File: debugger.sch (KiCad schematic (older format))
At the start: 7 parts, among them J2 USB_B_Micro, U7 STM32F042F6Px

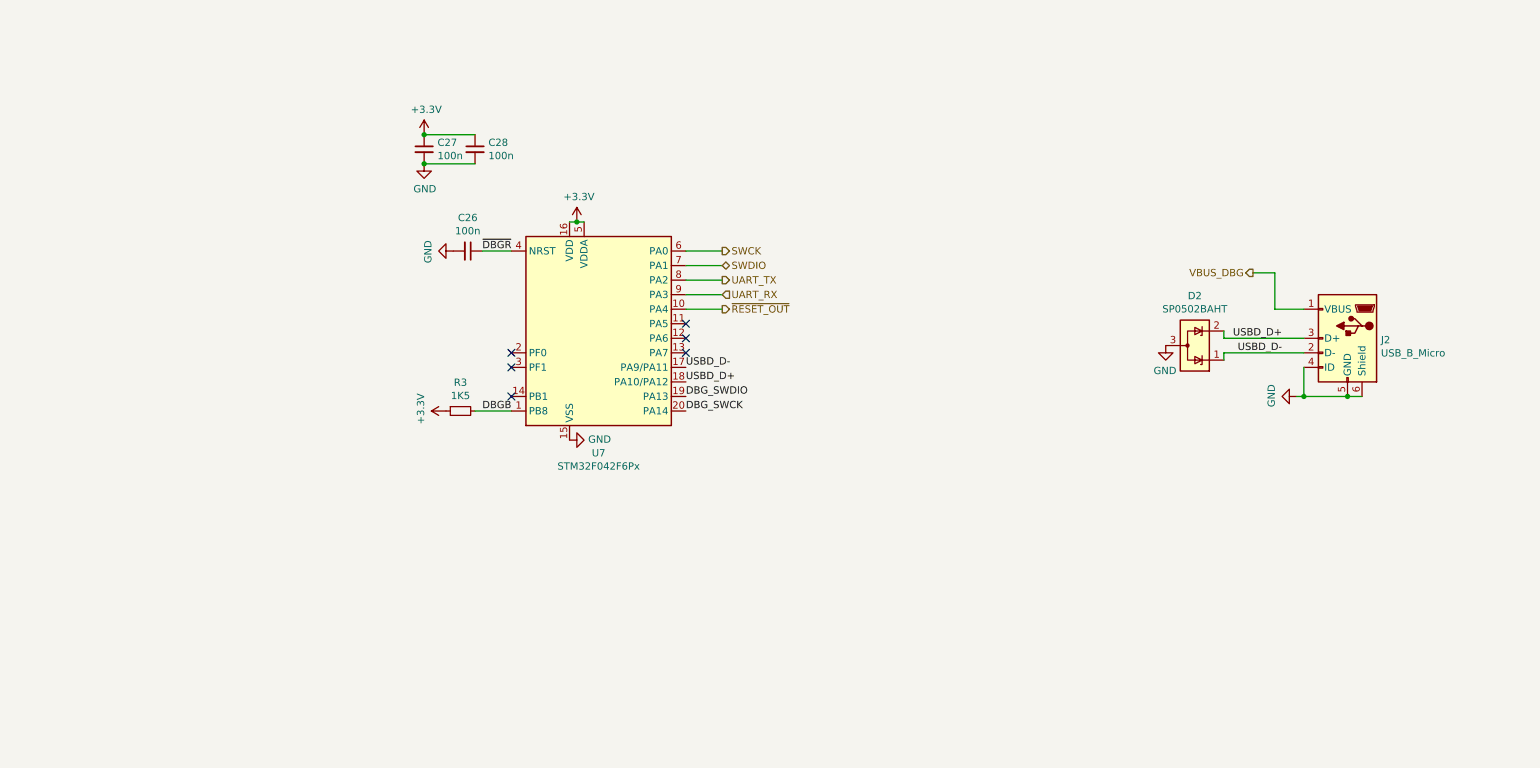
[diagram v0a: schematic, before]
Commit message: Add SWD connector for cortex-m7, SWD poggo pins and boot jumper for cmsis-dap mcu.
Signed-off-by: Martin Ribelotta <martinribelotta@gmail.com>
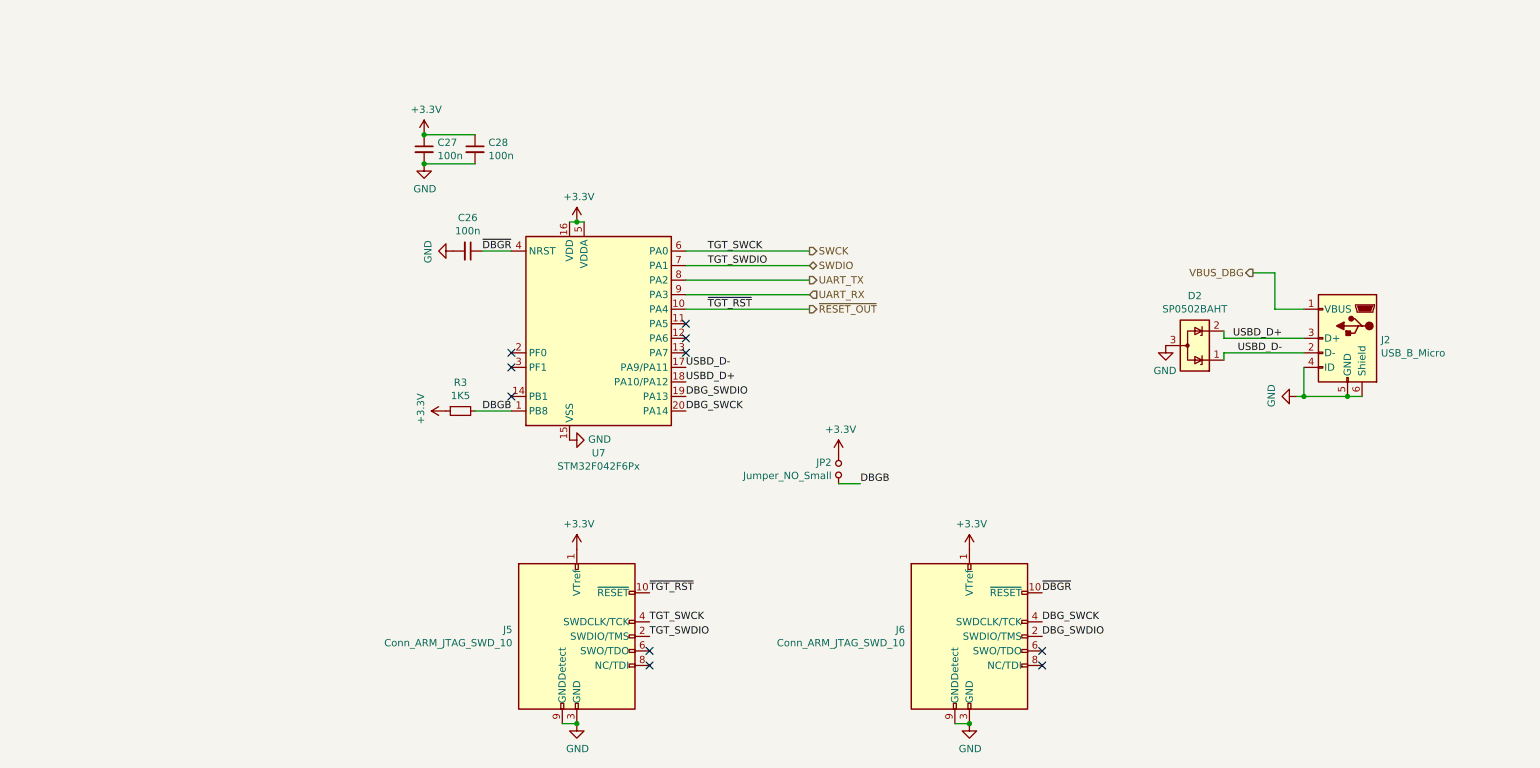
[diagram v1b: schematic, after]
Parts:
- added J5: Conn_ARM_JTAG_SWD_10, Connector_PinHeader_1.27mm:PinHeader_2x05_P1.27mm_Vertical_SMD, symbol Connector:Conn_ARM_JTAG_SWD_10
- added J6: Conn_ARM_JTAG_SWD_10, Connector:Tag-Connect_TC2050-IDC-NL_2x05_P1.27mm_Vertical, symbol Connector:Conn_ARM_JTAG_SWD_10
- added JP2: Jumper_NO_Small, Connector_PinHeader_2.54mm:PinHeader_1x02_P2.54mm_Vertical, symbol Device:Jumper_NO_Small
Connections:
- net +3V3: now also J5.1 (VTref), J6.1 (VTref), JP2.2
- net DBGB: now also JP2.1
- net DBG_SWCK: now also J6.4 (SWDCLK/TCK)
- net DBG_SWDIO: now also J6.2 (SWDIO/TMS)
- net GND: now also J5.3 (GND), J5.5 (GND), J5.9 (GNDDetect), J6.3 (GND), J6.5 (GND), J6.9 (GNDDetect)
- net SWCK: now also J5.4 (SWDCLK/TCK)
- net SWDIO: now also J5.2 (SWDIO/TMS)
- net ~DBGR: now also J6.10 (~RESET~)
- net ~RESET_OUT: now also J5.10 (~RESET~)
- no-connect marks 6 -> 10
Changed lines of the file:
@@
 	1    0    0    -1
 $EndComp
-Text HLabel 5400 2800 2    50   Output ~ 0
+Text HLabel 6000 2800 2    50   Output ~ 0
 SWCK
-Text HLabel 5400 2900 2    50   BiDi ~ 0
+Text HLabel 6000 2900 2    50   BiDi ~ 0
 SWDIO
-Wire Wire Line
-	5150 2800 5400 2800
-Wire Wire Line
-	5400 2900 5150 2900
-Text HLabel 5400 3000 2    50   Output ~ 0
+Text HLabel 6000 3000 2    50   Output ~ 0
 UART_TX
-Text HLabel 5400 3100 2    50   Input ~ 0
+Text HLabel 6000 3100 2    50   Input ~ 0
 UART_RX
-Wire Wire Line
-	5400 3000 5150 3000
-Wire Wire Line
-	5150 3100 5400 3100
 NoConn ~ 5150 3300
 NoConn ~ 5150 3400
-Text HLabel 5400 3200 2    50   Output ~ 0
+Text HLabel 6000 3200 2    50   Output ~ 0
 ~RESET_OUT
-Wire Wire Line
-	5400 3200 5150 3200
 NoConn ~ 5150 3500
 Text Label 5150 3700 0    50   ~ 0
@@
 Wire Wire Line
 	9200 3200 9400 3200
+Text Label 7600 5450 0    50   ~ 0
+DBG_SWDIO
+Text Label 7600 5350 0    50   ~ 0
+DBG_SWCK
+Text Label 7600 5150 0    50   ~ 0
+~DBGR
+Text Label 6350 4400 0    50   ~ 0
+DBGB
+$Comp
+L Device:Jumper_NO_Small JP2
+U 1 1 60341504
+P 6200 4300
+F 0 "JP2" V 6246 4348 50  0000 L CNN
+F 1 "Jumper_NO_Small" V 6155 4348 50  0000 L CNN
+F 2 "Connector_PinHeader_2.54mm:PinHeader_1x02_P2.54mm_Vertical" H 6200 4300 50  0001 C CNN
+F 3 "~" H 6200 4300 50  0001 C CNN
+	1    6200 4300
+	0    -1   -1   0
+$EndComp
+Wire Wire Line
+	6200 4400 6350 4400
+$Comp
+L power:+3V3 #PWR?
+U 1 1 60346736
+P 6200 4200
+AR Path="/60346736" Ref="#PWR?"  Part="1"
+AR Path="/60158DDC/60346736" Ref="#PWR052"  Part="1"
+F 0 "#PWR052" H 6200 4050 50  0001 C CNN
+F 1 "+3.3V" H 6215 4373 50  0000 C CNN
+F 2 "" H 6200 4200 50  0000 C CNN
+F 3 "" H 6200 4200 50  0000 C CNN
+	1    6200 4200
+	1    0    0    -1
+$EndComp
+$Comp
+L Connector:Conn_ARM_JTAG_SWD_10 J5
+U 1 1 60372EBF
+P 4400 5450
+F 0 "J5" H 3957 5496 50  0000 R CNN
+F 1 "Conn_ARM_JTAG_SWD_10" H 3957 5405 50  0000 R CNN
+F 2 "Connector_PinHeader_1.27mm:PinHeader_2x05_P1.27mm_Vertical_SMD" H 4400 5450 50  0001 C CNN
+F 3 "http://infocenter.arm.com/help/topic/com.arm.doc.ddi0314h/DDI0314H_coresight_components_trm.pdf" V 4050 4200 50  0001 C CNN
+	1    4400 5450
+	1    0    0    -1
+$EndComp
+$Comp
+L power:+3V3 #PWR?
+U 1 1 60372EC5
+P 4400 4850
+AR Path="/60372EC5" Ref="#PWR?"  Part="1"
+AR Path="/60158DDC/60372EC5" Ref="#PWR026"  Part="1"
+F 0 "#PWR026" H 4400 4700 50  0001 C CNN
+F 1 "+3.3V" H 4415 5023 50  0000 C CNN
+F 2 "" H 4400 4850 50  0000 C CNN
+F 3 "" H 4400 4850 50  0000 C CNN
+	1    4400 4850
+	1    0    0    -1
+$EndComp
+$Comp
+L power:GND #PWR?
+U 1 1 60372ECB
+P 4400 6050
+AR Path="/60372ECB" Ref="#PWR?"  Part="1"
+AR Path="/60158DDC/60372ECB" Ref="#PWR029"  Part="1"
+F 0 "#PWR029" H 4400 5800 50  0001 C CNN
+F 1 "GND" H 4405 5877 50  0000 C CNN
+F 2 "" H 4400 6050 50  0000 C CNN
+F 3 "" H 4400 6050 50  0000 C CNN
+	1    4400 6050
+	1    0    0    -1
+$EndComp
+Wire Wire Line
+	4300 6050 4400 6050
+Connection ~ 4400 6050
+Wire Wire Line
+	5150 2800 6000 2800
+Wire Wire Line
+	5150 2900 6000 2900
+Wire Wire Line
+	5150 3000 6000 3000
+Wire Wire Line
+	5150 3100 6000 3100
+Wire Wire Line
+	5150 3200 6000 3200
+Text Label 5300 2800 0    50   ~ 0
+TGT_SWCK
+Text Label 5300 2900 0    50   ~ 0
+TGT_SWDIO
+Text Label 5300 3200 0    50   ~ 0
+~TGT_RST
+Text Label 4900 5350 0    50   ~ 0
+TGT_SWCK
+Text Label 4900 5450 0    50   ~ 0
+TGT_SWDIO
+NoConn ~ 4900 5550
+NoConn ~ 4900 5650
+Text Label 4900 5150 0    50   ~ 0
+~TGT_RST
+$Comp
+L Connector:Conn_ARM_JTAG_SWD_10 J6
+U 1 1 6037A7B7
+P 7100 5450
+F 0 "J6" H 6657 5496 50  0000 R CNN
+F 1 "Conn_ARM_JTAG_SWD_10" H 6657 5405 50  0000 R CNN
+F 2 "Connector:Tag-Connect_TC2050-IDC-NL_2x05_P1.27mm_Vertical" H 7100 5450 50  0001 C CNN
+F 3 "http://infocenter.arm.com/help/topic/com.arm.doc.ddi0314h/DDI0314H_coresight_components_trm.pdf" V 6750 4200 50  0001 C CNN
+	1    7100 5450
+	1    0    0    -1
+$EndComp
+NoConn ~ 7600 5550
+NoConn ~ 7600 5650
+$Comp
+L power:GND #PWR?
+U 1 1 6038215C
+P 7100 6050
+AR Path="/6038215C" Ref="#PWR?"  Part="1"
+AR Path="/60158DDC/6038215C" Ref="#PWR061"  Part="1"
+F 0 "#PWR061" H 7100 5800 50  0001 C CNN
+F 1 "GND" H 7105 5877 50  0000 C CNN
+F 2 "" H 7100 6050 50  0000 C CNN
+F 3 "" H 7100 6050 50  0000 C CNN
+	1    7100 6050
+	1    0    0    -1
+$EndComp
+Wire Wire Line
+	7100 6050 7000 6050
+Connection ~ 7100 6050
+$Comp
+L power:+3V3 #PWR?
+U 1 1 60383929
+P 7100 4850
+AR Path="/60383929" Ref="#PWR?"  Part="1"
+AR Path="/60158DDC/60383929" Ref="#PWR053"  Part="1"
+F 0 "#PWR053" H 7100 4700 50  0001 C CNN
+F 1 "+3.3V" H 7115 5023 50  0000 C CNN
+F 2 "" H 7100 4850 50  0000 C CNN
+F 3 "" H 7100 4850 50  0000 C CNN
+	1    7100 4850
+	1    0    0    -1
+$EndComp
 $EndSCHEMATC

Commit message: Replace non stocked components.
 - Redesign 5V/3.3V using TPS6216xDSGT
 - Use bigger crystal (move to 5031 case)
 - Change some components parts

Signed-off-by: Martin Ribelotta <martinribelotta@gmail.com>
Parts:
- C26, C27, C28: DESCRIPTION (none) -> Capacitor 100n 0603
- D2: DESCRIPTION (none) -> SP0502BAHT
- J2: DESCRIPTION (none) -> USB Micro B Molex 47346-0001
- R3: DESCRIPTION (none) -> Resistor 1.5K 0603
- U7: DESCRIPTION (none) -> STM32F042F6P*
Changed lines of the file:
@@
 F 2 "Package_SO:TSSOP-20_4.4x6.5mm_P0.65mm" H 4050 2600 50  0001 R CNN
 F 3 "http://www.st.com/st-web-ui/static/active/en/resource/technical/document/datasheet/DM00105814.pdf" H 4550 3300 50  0001 C CNN
+F 4 "STM32F042F6P*" H 4550 3300 50  0001 C CNN "DESCRIPTION"
 	1    4550 3300
 	1    0    0    -1
@@
 F 2 "Package_TO_SOT_SMD:SOT-23" H 8875 3400 50  0001 L CNN
 F 3 "http://www.littelfuse.com/~/media/files/littelfuse/technical%20resources/documents/data%20sheets/sp05xxba.pdf" H 8775 3575 50  0001 C CNN
+F 4 "SP0502BAHT" H 8650 3450 50  0001 C CNN "DESCRIPTION"
 	1    8650 3450
 	0    1    -1   0
@@
 F 2 "Capacitor_SMD:C_0603_1608Metric" H 3350 2100 50  0001 C CNN
 F 3 "~" H 3350 2100 50  0001 C CNN
+F 4 "Capacitor 100n 0603" H 3350 2100 50  0001 C CNN "DESCRIPTION"
 	1    3350 2100
 	1    0    0    -1
@@
 F 2 "Capacitor_SMD:C_0603_1608Metric" H 3700 2100 50  0001 C CNN
 F 3 "~" H 3700 2100 50  0001 C CNN
+F 4 "Capacitor 100n 0603" H 3700 2100 50  0001 C CNN "DESCRIPTION"
 	1    3700 2100
 	1    0    0    -1
@@
 F 2 "Capacitor_SMD:C_0603_1608Metric" H 3650 2800 50  0001 C CNN
 F 3 "~" H 3650 2800 50  0001 C CNN
+F 4 "Capacitor 100n 0603" H 3650 2800 50  0001 C CNN "DESCRIPTION"
 	1    3650 2800
 	0    1    -1   0
@@
 F 2 "Resistor_SMD:R_0603_1608Metric" H 3600 3900 50  0001 C CNN
 F 3 "~" H 3600 3900 50  0001 C CNN
+F 4 "Resistor 1.5K 0603" H 3600 3900 50  0001 C CNN "DESCRIPTION"
 	1    3600 3900
 	0    -1   1    0
@@
 F 2 "Connector_USB:USB_Micro-B_Molex_47346-0001" H 9850 3350 50  0001 C CNN
 F 3 "~" H 9850 3350 50  0001 C CNN
+F 4 "USB Micro B Molex 47346-0001" H 9700 3400 50  0001 C CNN "DESCRIPTION"
 	1    9700 3400
 	-1   0    0    -1

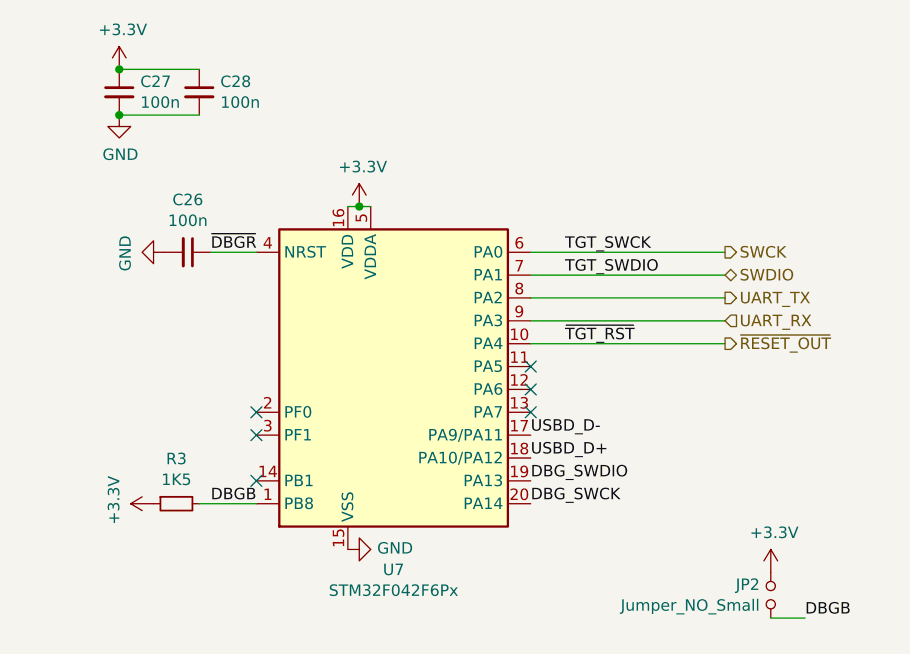
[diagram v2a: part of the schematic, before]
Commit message: Fix in design:
 - Add r-series to QSPI interfaces
 - Change vCAP from 100n to 2.2u
 - Add pullup to SWCK/DIO and nRST
 - Remove AGND/DGND separation

Signed-off-by: Martin Ribelotta <martinribelotta@gmail.com>
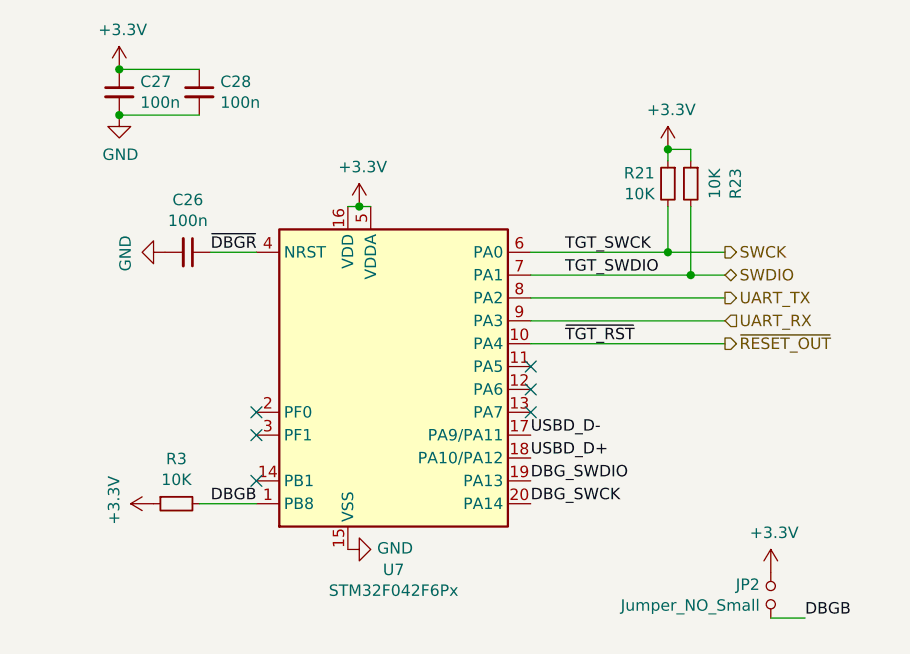
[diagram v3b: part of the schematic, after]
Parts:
- added R21, R23: 10K, Resistor_SMD:R_0603_1608Metric, symbol Device:R_Small
- R3: value 1K5 -> 10K
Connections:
- net +3V3: now also R21.1, R23.1
- net SWCK: now also R21.2
- net SWDIO: now also R23.2
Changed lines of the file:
@@
 AR Path="/60158DDC/60189E41" Ref="R3"  Part="1"
 F 0 "R3" V 3404 3900 50  0000 C CNN
-F 1 "1K5" V 3495 3900 50  0000 C CNN
+F 1 "10K" V 3495 3900 50  0000 C CNN
 F 2 "Resistor_SMD:R_0603_1608Metric" H 3600 3900 50  0001 C CNN
 F 3 "~" H 3600 3900 50  0001 C CNN
@@
 Connection ~ 4400 6050
 Wire Wire Line
-	5150 2800 6000 2800
-Wire Wire Line
-	5150 2900 6000 2900
+	5150 2800 5750 2800
+Wire Wire Line
+	5150 2900 5850 2900
 Wire Wire Line
 	5150 3000 6000 3000
@@
 	1    0    0    -1
 $EndComp
+$Comp
+L Device:R_Small R?
+U 1 1 605A9B9C
+P 5850 2500
+AR Path="/605A9B9C" Ref="R?"  Part="1"
+AR Path="/60158DDC/605A9B9C" Ref="R23"  Part="1"
+F 0 "R23" V 5654 2500 50  0000 C CNN
+F 1 "10K" V 5745 2500 50  0000 C CNN
+F 2 "Resistor_SMD:R_0603_1608Metric" H 5850 2500 50  0001 C CNN
+F 3 "~" H 5850 2500 50  0001 C CNN
+F 4 "Resistor 1.5K 0603" H 5850 2500 50  0001 C CNN "DESCRIPTION"
+	1    5850 2500
+	-1   0    0    -1
+$EndComp
+$Comp
+L Device:R_Small R?
+U 1 1 605ABFAC
+P 5750 2500
+AR Path="/605ABFAC" Ref="R?"  Part="1"
+AR Path="/60158DDC/605ABFAC" Ref="R21"  Part="1"
+F 0 "R21" H 5808 2546 50  0000 L CNN
+F 1 "10K" H 5808 2455 50  0000 L CNN
+F 2 "Resistor_SMD:R_0603_1608Metric" H 5750 2500 50  0001 C CNN
+F 3 "~" H 5750 2500 50  0001 C CNN
+F 4 "Resistor 1.5K 0603" H 5750 2500 50  0001 C CNN "DESCRIPTION"
+	1    5750 2500
+	-1   0    0    -1
+$EndComp
+Wire Wire Line
+	5750 2600 5750 2800
+Connection ~ 5750 2800
+Wire Wire Line
+	5750 2800 6000 2800
+Wire Wire Line
+	5850 2600 5850 2900
+Connection ~ 5850 2900
+Wire Wire Line
+	5850 2900 6000 2900
+$Comp
+L power:+3V3 #PWR?
+U 1 1 60617550
+P 5750 2350
+AR Path="/60617550" Ref="#PWR?"  Part="1"
+AR Path="/60158DDC/60617550" Ref="#PWR0115"  Part="1"
+F 0 "#PWR0115" H 5750 2200 50  0001 C CNN
+F 1 "+3.3V" H 5765 2523 50  0000 C CNN
+F 2 "" H 5750 2350 50  0000 C CNN
+F 3 "" H 5750 2350 50  0000 C CNN
+	1    5750 2350
+	1    0    0    -1
+$EndComp
+Wire Wire Line
+	5750 2400 5750 2350
+Wire Wire Line
+	5750 2350 5850 2350
+Wire Wire Line
+	5850 2350 5850 2400
+Connection ~ 5750 2350
 $EndSCHEMATC

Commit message: Add new BOM to octopart
TODO: PSRAM is not recognized by Octopart but is available in LCSC

Signed-off-by: Martin Ribelotta <martinribelotta@gmail.com>
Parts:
- C26, C27, C28: MANUFACTURER (none) -> Yageo; MANUFACTURER_PART_NUMBER (none) -> CC0603KRX7R9BB104
- D2: MANUFACTURER (none) -> Littlelfuse; MANUFACTURER_PART_NUMBER (none) -> SP0502BAHTG
- J2: MANUFACTURER (none) -> Molex; MANUFACTURER_PART_NUMBER (none) -> 47346-0001
- R21, R23, R3: MANUFACTURER (none) -> Yageo; MANUFACTURER_PART_NUMBER (none) -> RC0603FR-0710KL
- U7: MANUFACTURER (none) -> ST; MANUFACTURER_PART_NUMBER (none) -> STM32F042F6Px
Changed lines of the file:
@@
 F 3 "http://www.st.com/st-web-ui/static/active/en/resource/technical/document/datasheet/DM00105814.pdf" H 4550 3300 50  0001 C CNN
 F 4 "STM32F042F6P*" H 4550 3300 50  0001 C CNN "DESCRIPTION"
+F 5 "ST" H 4550 3300 50  0001 C CNN "MANUFACTURER"
+F 6 "STM32F042F6Px" H 4550 3300 50  0001 C CNN "MANUFACTURER_PART_NUMBER"
 	1    4550 3300
 	1    0    0    -1
@@
 F 3 "http://www.littelfuse.com/~/media/files/littelfuse/technical%20resources/documents/data%20sheets/sp05xxba.pdf" H 8775 3575 50  0001 C CNN
 F 4 "SP0502BAHT" H 8650 3450 50  0001 C CNN "DESCRIPTION"
+F 5 "Littlelfuse" H 8650 3450 50  0001 C CNN "MANUFACTURER"
+F 6 "SP0502BAHTG" H 8650 3450 50  0001 C CNN "MANUFACTURER_PART_NUMBER"
 	1    8650 3450
 	0    1    -1   0
@@
 F 3 "~" H 3350 2100 50  0001 C CNN
 F 4 "Capacitor 100n 0603" H 3350 2100 50  0001 C CNN "DESCRIPTION"
+F 5 "CC0603KRX7R9BB104" H 3350 2100 50  0001 C CNN "MANUFACTURER_PART_NUMBER"
+F 6 "Yageo" H 3350 2100 50  0001 C CNN "MANUFACTURER"
 	1    3350 2100
 	1    0    0    -1
@@
 F 3 "~" H 3700 2100 50  0001 C CNN
 F 4 "Capacitor 100n 0603" H 3700 2100 50  0001 C CNN "DESCRIPTION"
+F 5 "CC0603KRX7R9BB104" H 3700 2100 50  0001 C CNN "MANUFACTURER_PART_NUMBER"
+F 6 "Yageo" H 3700 2100 50  0001 C CNN "MANUFACTURER"
 	1    3700 2100
 	1    0    0    -1
@@
 F 3 "~" H 3650 2800 50  0001 C CNN
 F 4 "Capacitor 100n 0603" H 3650 2800 50  0001 C CNN "DESCRIPTION"
+F 5 "CC0603KRX7R9BB104" H 3650 2800 50  0001 C CNN "MANUFACTURER_PART_NUMBER"
+F 6 "Yageo" H 3650 2800 50  0001 C CNN "MANUFACTURER"
 	1    3650 2800
 	0    1    -1   0
@@
 F 3 "~" H 3600 3900 50  0001 C CNN
 F 4 "Resistor 1.5K 0603" H 3600 3900 50  0001 C CNN "DESCRIPTION"
+F 5 "Yageo" H 3600 3900 50  0001 C CNN "MANUFACTURER"
+F 6 "RC0603FR-0710KL" H 3600 3900 50  0001 C CNN "MANUFACTURER_PART_NUMBER"
 	1    3600 3900
 	0    -1   1    0
@@
 F 3 "~" H 9850 3350 50  0001 C CNN
 F 4 "USB Micro B Molex 47346-0001" H 9700 3400 50  0001 C CNN "DESCRIPTION"
+F 5 "Molex" H 9700 3400 50  0001 C CNN "MANUFACTURER"
+F 6 "47346-0001" H 9700 3400 50  0001 C CNN "MANUFACTURER_PART_NUMBER"
 	1    9700 3400
 	-1   0    0    -1
@@
 F 3 "~" H 5850 2500 50  0001 C CNN
 F 4 "Resistor 1.5K 0603" H 5850 2500 50  0001 C CNN "DESCRIPTION"
+F 5 "Yageo" H 5850 2500 50  0001 C CNN "MANUFACTURER"
+F 6 "RC0603FR-0710KL" H 5850 2500 50  0001 C CNN "MANUFACTURER_PART_NUMBER"
 	1    5850 2500
 	-1   0    0    -1
@@
 F 3 "~" H 5750 2500 50  0001 C CNN
 F 4 "Resistor 1.5K 0603" H 5750 2500 50  0001 C CNN "DESCRIPTION"
+F 5 "Yageo" H 5750 2500 50  0001 C CNN "MANUFACTURER"
+F 6 "RC0603FR-0710KL" H 5750 2500 50  0001 C CNN "MANUFACTURER_PART_NUMBER"
 	1    5750 2500
 	-1   0    0    -1
